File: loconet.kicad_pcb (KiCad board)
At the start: 2 copper layers, 79.4 x 91.6 mm, 51 parts, among them CON1 BARREL_JACK, J1 RJ12, J2 RJ12, J3 RJ12, J4 RJ12, J5 RJ12, J6 RJ12, P1 CONN_01X04, P10 CONN_01X04, P2 CONN_01X04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

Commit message: Small fixes
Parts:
- C1, C2: footprint Capacitors_ThroughHole:C_Rect_L7_W6_P5 -> Capacitors_THT:C_Rect_L7.2mm_W5.5mm_P5.00mm_FKS2_FKP2_MKS2_MKP2
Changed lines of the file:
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@@
   (general
     (links 104)
-    (no_connects 2)
+    (no_connects 0)
     (area 113.949999 60.949999 193.500001 152.600001)
     (thickness 1.6)
@@
     (fp_circle (center 0 0) (end 3 0) (layer Cmts.User) (width 0.381))
     (pad 1 thru_hole circle (at 0 0) (size 3 3) (drill 3) (layers))
-  )
-  (module Capacitors_ThroughHole:C_Rect_L7_W6_P5 (layer F.Cu)
-    (at 156.75 139.5 90)
-    (descr "Film Capacitor Length 7mm x Width 6mm")
-    (tags Capacitor)
-    (fp_text reference C1 (at 7.5 0 180) (layer F.SilkS)
-      (effects (font (size 1 1) (thickness 0.15)))
-    )
-    (fp_text value C (at 2.5 4.25 90) (layer F.Fab)
-      (effects (font (size 1 1) (thickness 0.15)))
-    )
-    (fp_line (start -1.25 -3.25) (end 6.25 -3.25) (layer F.CrtYd) (width 0.05))
-    (fp_line (start 6.25 -3.25) (end 6.25 3.25) (layer F.CrtYd) (width 0.05))
-    (fp_line (start 6.25 3.25) (end -1.25 3.25) (layer F.CrtYd) (width 0.05))
-    (fp_line (start -1.25 3.25) (end -1.25 -3.25) (layer F.CrtYd) (width 0.05))
-    (fp_line (start -1 -3) (end 6 -3) (layer F.SilkS) (width 0.15))
-    (fp_line (start 6 -3) (end 6 3) (layer F.SilkS) (width 0.15))
-    (fp_line (start 6 3) (end -1 3) (layer F.SilkS) (width 0.15))
-    (fp_line (start -1 3) (end -1 -3) (layer F.SilkS) (width 0.15))
-    (pad 1 thru_hole rect (at 0 0 90) (size 1.3 1.3) (drill 0.8) (layers *.Cu *.Mask F.SilkS)
-      (net 13 +12V))
-    (pad 2 thru_hole circle (at 5 0 90) (size 1.3 1.3) (drill 0.8) (layers *.Cu *.Mask F.SilkS)
-      (net 2 GND))
-    (model Capacitors_ThroughHole.3dshapes/C_Rect_L7_W6_P5.wrl
-      (at (xyz 0.098425 0 0))
-      (scale (xyz 1 1 1))
-      (rotate (xyz 0 0 0))
-    )
-  )
-  (module Capacitors_ThroughHole:C_Rect_L7_W6_P5 (layer F.Cu)
-    (at 163.5 139.5 90)
-    (descr "Film Capacitor Length 7mm x Width 6mm")
-    (tags Capacitor)
-    (fp_text reference C2 (at 7.5 0 180) (layer F.SilkS)
-      (effects (font (size 1 1) (thickness 0.15)))
-    )
-    (fp_text value C (at 2.5 4.25 90) (layer F.Fab)
-      (effects (font (size 1 1) (thickness 0.15)))
-    )
-    (fp_line (start -1.25 -3.25) (end 6.25 -3.25) (layer F.CrtYd) (width 0.05))
-    (fp_line (start 6.25 -3.25) (end 6.25 3.25) (layer F.CrtYd) (width 0.05))
-    (fp_line (start 6.25 3.25) (end -1.25 3.25) (layer F.CrtYd) (width 0.05))
-    (fp_line (start -1.25 3.25) (end -1.25 -3.25) (layer F.CrtYd) (width 0.05))
-    (fp_line (start -1 -3) (end 6 -3) (layer F.SilkS) (width 0.15))
-    (fp_line (start 6 -3) (end 6 3) (layer F.SilkS) (width 0.15))
-    (fp_line (start 6 3) (end -1 3) (layer F.SilkS) (width 0.15))
-    (fp_line (start -1 3) (end -1 -3) (layer F.SilkS) (width 0.15))
-    (pad 1 thru_hole rect (at 0 0 90) (size 1.3 1.3) (drill 0.8) (layers *.Cu *.Mask F.SilkS)
-      (net 5 +5V))
-    (pad 2 thru_hole circle (at 5 0 90) (size 1.3 1.3) (drill 0.8) (layers *.Cu *.Mask F.SilkS)
-      (net 2 GND))
-    (model Capacitors_ThroughHole.3dshapes/C_Rect_L7_W6_P5.wrl
-      (at (xyz 0.098425 0 0))
-      (scale (xyz 1 1 1))
-      (rotate (xyz 0 0 0))
-    )
   )
   (module Symbols:Symbol_CC-Attribution_CopperTop_Small (layer F.Cu)
@@
       (net 3 Railsync-))
     (model ${KISYS3DMOD}/Pin_Headers.3dshapes/Pin_Header_Straight_1x02_Pitch2.54mm.wrl
-      (at (xyz 0 -0.05 0))
+      (at (xyz 0 -0 0))
       (scale (xyz 1 1 1))
-      (rotate (xyz 0 0 90))
+      (rotate (xyz 0 0 0))
     )
   )
@@
       (net 4 Railsync+))
     (model ${KISYS3DMOD}/Pin_Headers.3dshapes/Pin_Header_Straight_1x02_Pitch2.54mm.wrl
-      (at (xyz 0 -0.05 0))
+      (at (xyz 0 0 0))
       (scale (xyz 1 1 1))
-      (rotate (xyz 0 0 90))
+      (rotate (xyz 0 0 0))
     )
   )
@@
       (net 2 GND))
   )
+  (module Capacitors_THT:C_Rect_L7.2mm_W5.5mm_P5.00mm_FKS2_FKP2_MKS2_MKP2 (layer F.Cu)
+    (at 163.5 139.5 90)
+    (descr "C, Rect series, Radial, pin pitch=5.00mm, , length*width=7.2*5.5mm^2, Capacitor, http://www.wima.com/EN/WIMA_FKS_2.pdf")
+    (tags "C Rect series Radial pin pitch 5.00mm  length 7.2mm width 5.5mm Capacitor")
+    (fp_text reference C2 (at 2.5 -3.81 90) (layer F.SilkS)
+      (effects (font (size 1 1) (thickness 0.15)))
+    )
+    (fp_text value C (at 2.5 3.81 90) (layer F.Fab)
+      (effects (font (size 1 1) (thickness 0.15)))
+    )
+    (fp_line (start -1.1 -2.75) (end -1.1 2.75) (layer F.Fab) (width 0.1))
+    (fp_line (start -1.1 2.75) (end 6.1 2.75) (layer F.Fab) (width 0.1))
+    (fp_line (start 6.1 2.75) (end 6.1 -2.75) (layer F.Fab) (width 0.1))
+    (fp_line (start 6.1 -2.75) (end -1.1 -2.75) (layer F.Fab) (width 0.1))
+    (fp_line (start -1.16 -2.81) (end 6.16 -2.81) (layer F.SilkS) (width 0.12))
+    (fp_line (start -1.16 2.81) (end 6.16 2.81) (layer F.SilkS) (width 0.12))
+    (fp_line (start -1.16 -2.81) (end -1.16 2.81) (layer F.SilkS) (width 0.12))
+    (fp_line (start 6.16 -2.81) (end 6.16 2.81) (layer F.SilkS) (width 0.12))
+    (fp_line (start -1.45 -3.1) (end -1.45 3.1) (layer F.CrtYd) (width 0.05))
+    (fp_line (start -1.45 3.1) (end 6.45 3.1) (layer F.CrtYd) (width 0.05))
+    (fp_line (start 6.45 3.1) (end 6.45 -3.1) (layer F.CrtYd) (width 0.05))
+    (fp_line (start 6.45 -3.1) (end -1.45 -3.1) (layer F.CrtYd) (width 0.05))
+    (pad 1 thru_hole circle (at 0 0 90) (size 1.6 1.6) (drill 0.8) (layers *.Cu *.Mask)
+      (net 5 +5V))
+    (pad 2 thru_hole circle (at 5 0 90) (size 1.6 1.6) (drill 0.8) (layers *.Cu *.Mask)
+      (net 2 GND))
+    (model Capacitors_THT.3dshapes/C_Rect_L7.2mm_W5.5mm_P5.00mm_FKS2_FKP2_MKS2_MKP2.wrl
+      (at (xyz 0 0 0))
+      (scale (xyz 0 0 0))
+      (rotate (xyz 0 0 0))
+    )
+  )
+  (module Capacitors_THT:C_Rect_L7.2mm_W5.5mm_P5.00mm_FKS2_FKP2_MKS2_MKP2 (layer F.Cu)
+    (at 156.75 139.5 90)
+    (descr "C, Rect series, Radial, pin pitch=5.00mm, , length*width=7.2*5.5mm^2, Capacitor, http://www.wima.com/EN/WIMA_FKS_2.pdf")
+    (tags "C Rect series Radial pin pitch 5.00mm  length 7.2mm width 5.5mm Capacitor")
+    (fp_text reference C1 (at 2.5 -3.81 90) (layer F.SilkS)
+      (effects (font (size 1 1) (thickness 0.15)))
+    )
+    (fp_text value C (at 2.5 3.81 90) (layer F.Fab)
+      (effects (font (size 1 1) (thickness 0.15)))
+    )
+    (fp_line (start -1.1 -2.75) (end -1.1 2.75) (layer F.Fab) (width 0.1))
+    (fp_line (start -1.1 2.75) (end 6.1 2.75) (layer F.Fab) (width 0.1))
+    (fp_line (start 6.1 2.75) (end 6.1 -2.75) (layer F.Fab) (width 0.1))
+    (fp_line (start 6.1 -2.75) (end -1.1 -2.75) (layer F.Fab) (width 0.1))
+    (fp_line (start -1.16 -2.81) (end 6.16 -2.81) (layer F.SilkS) (width 0.12))
+    (fp_line (start -1.16 2.81) (end 6.16 2.81) (layer F.SilkS) (width 0.12))
+    (fp_line (start -1.16 -2.81) (end -1.16 2.81) (layer F.SilkS) (width 0.12))
+    (fp_line (start 6.16 -2.81) (end 6.16 2.81) (layer F.SilkS) (width 0.12))
+    (fp_line (start -1.45 -3.1) (end -1.45 3.1) (layer F.CrtYd) (width 0.05))
+    (fp_line (start -1.45 3.1) (end 6.45 3.1) (layer F.CrtYd) (width 0.05))
+    (fp_line (start 6.45 3.1) (end 6.45 -3.1) (layer F.CrtYd) (width 0.05))
+    (fp_line (start 6.45 -3.1) (end -1.45 -3.1) (layer F.CrtYd) (width 0.05))
+    (pad 1 thru_hole circle (at 0 0 90) (size 1.6 1.6) (drill 0.8) (layers *.Cu *.Mask)
+      (net 13 +12V))
+    (pad 2 thru_hole circle (at 5 0 90) (size 1.6 1.6) (drill 0.8) (layers *.Cu *.Mask)
+      (net 2 GND))
+    (model Capacitors_THT.3dshapes/C_Rect_L7.2mm_W5.5mm_P5.00mm_FKS2_FKP2_MKS2_MKP2.wrl
+      (at (xyz 0 0 0))
+      (scale (xyz 0 0 0))
+      (rotate (xyz 0 0 0))
+    )
+  )
   (gr_text http://bit.ly/1HuogNj (at 159 137) (layer B.SilkS)

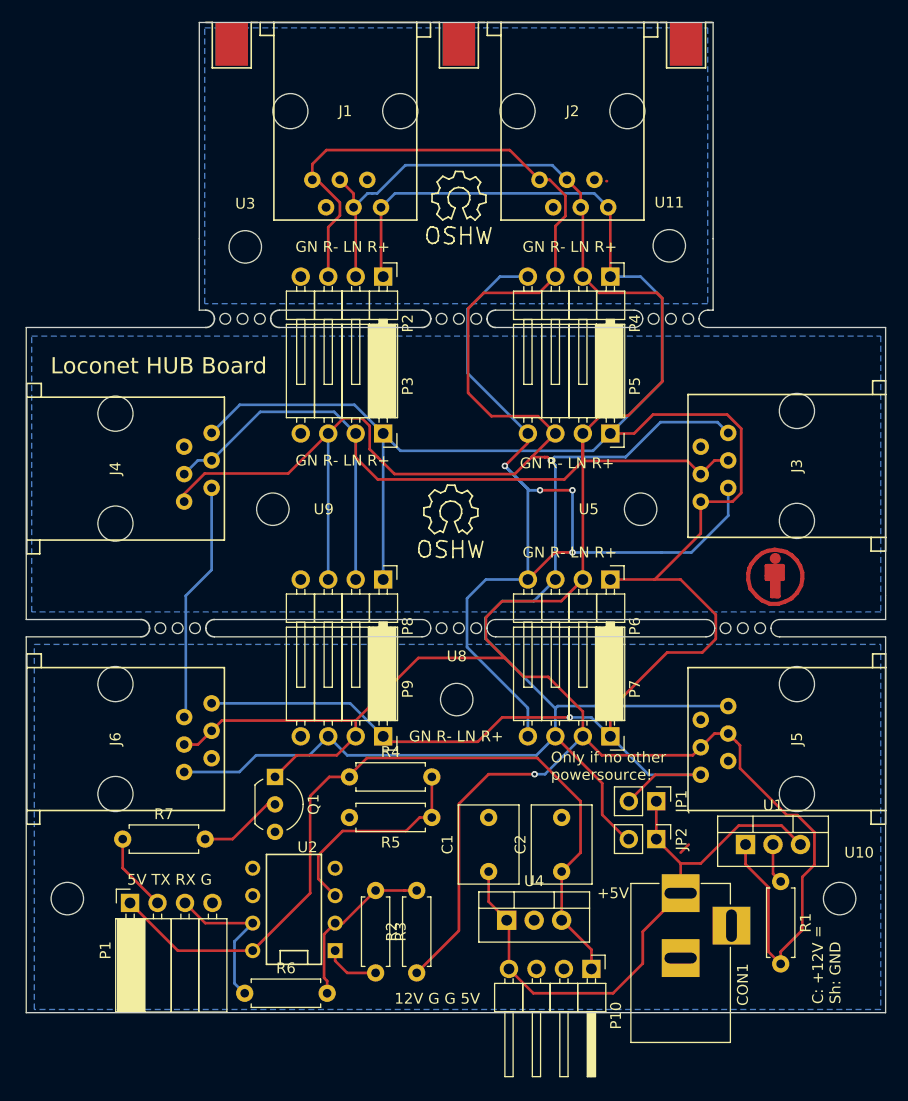
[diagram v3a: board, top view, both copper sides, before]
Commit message: Started update to kicad 8
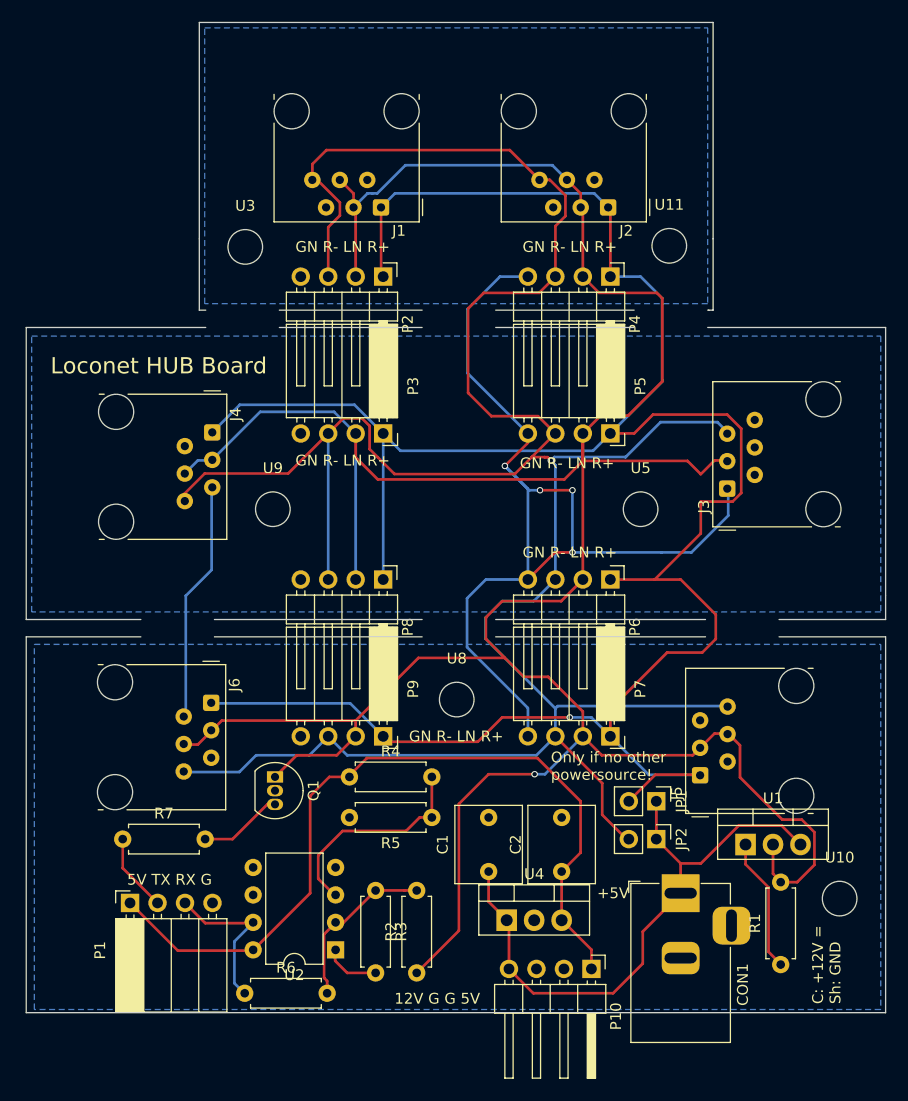
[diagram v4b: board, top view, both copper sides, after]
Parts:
- removed REF** (x3): Solder_board_connect_3x3, Connectors:Solder_board_connect_3x3
- removed REF**: MountingHole_3mm, Mounting_Holes:MountingHole_3mm
- removed REF**: Symbol_CC-Attribution_CopperTop_Small, Symbols:Symbol_CC-Attribution_CopperTop_Small
- removed REF** (x2): Symbol_OSHW-Logo_SilkScreen, Symbols:Symbol_OSHW-Logo_SilkScreen
- removed REF** (x6): Mousebite, Other:Mousebite
- C1, C2: footprint Capacitors_THT:C_Rect_L7.2mm_W5.5mm_P5.00mm_FKS2_FKP2_MKS2_MKP2 -> Capacitor_THT:C_Rect_L7.0mm_W6.0mm_P5.00mm
- CON1: footprint Connectors:BARREL_JACK -> Connector_BarrelJack:BarrelJack_Horizontal
- J1, J2, J3, J4, J5, J6: footprint Connectors:RJ12_horizontal -> Connector_RJ:RJ12_Amphenol_54601-x06_Horizontal
- JP1, JP2: footprint Pin_Headers:Pin_Header_Straight_1x02_Pitch2.54mm -> Connector_PinHeader_2.54mm:PinHeader_1x02_P2.54mm_Vertical
- P1, P3, P5, P7, P9: footprint Socket_Strips:Socket_Strip_Angled_1x04_Pitch2.54mm -> Connector_PinSocket_2.54mm:PinSocket_1x04_P2.54mm_Horizontal
- P10, P2, P4, P6, P8: footprint Pin_Headers:Pin_Header_Angled_1x04_Pitch2.54mm -> Connector_PinHeader_2.54mm:PinHeader_1x04_P2.54mm_Horizontal
- Q1: footprint TO_SOT_Packages_THT:TO-92_Inline_Wide -> Package_TO_SOT_THT:TO-92_Inline
- R1, R2, R3, R4, R5, R6, R7: footprint Resistors_THT:R_Axial_DIN0207_L6.3mm_D2.5mm_P7.62mm_Horizontal -> Resistor_THT:R_Axial_DIN0207_L6.3mm_D2.5mm_P7.62mm_Horizontal
- U1, U4: footprint TO_SOT_Packages_THT:TO-220_Vertical -> Package_TO_SOT_THT:TO-220-3_Vertical
- U10, U11, U3, U5, U8, U9: footprint Mounting_Holes:MountingHole_3mm -> MountingHole:MountingHole_3.2mm_M3_DIN965
- U2: footprint Housings_DIP:DIP-8__300 -> Package_DIP:DIP-8_W7.62mm
- moved J4 9.56 mm to (131.2, 98.9)
- moved J5 9.56 mm to (176.3, 130.6)
- moved J1 9.49 mm to (146.8, 78.1)
- moved J2 9.49 mm to (167.8, 78.1)
- moved J6 9.46 mm to (131.1, 123.9)
- moved R1 7.68 mm to (183.8, 148.1), turned to 90 degrees
- moved J3 6.77 mm to (178.8, 104.1)
- moved U2 5.37 mm to (142.6, 146.7), turned to 180 degrees
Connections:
- CON1 pad 3: GND -> (no net)
- R1 pad 1: Net-(R1-Pad1) -> GND
- U1 pad 1: Loconet -> GND
- U1 pad 2: Net-(R1-Pad1) -> Loconet
- U2 pad 5: Net-(U2-Pad5) -> unconnected-(U2-BAL-Pad5)
- U2 pad 6: Net-(U2-Pad6) -> unconnected-(U2-STRB-Pad6)
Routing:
- net Railsync+: track 227.2 -> 321.0 mm, vias 1 -> 5
- net GND: track 121.2 -> 39.8 mm, vias 4 -> 0
- net Loconet: track 309.5 -> 294.7 mm
- net Net-(Q1-B): track 7.79 -> 0.00 mm
- net (no net): track 1.12 -> 7.79 mm
- net Net-(R1-Pad1): track 3.71 -> 0.00 mm
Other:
- outline, holes or cut-outs redrawn
- net class Default removed
- net class Small removed
